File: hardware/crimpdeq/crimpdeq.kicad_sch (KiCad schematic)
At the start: 54 parts, among them J2 USB4105-GF-A, Q1 S8550, Q2 DMG3415U, SW1 SW_Push, SW2 SW_Push, U1 ESP32-C3-MINI-1, U2 MCP73831T-2ACI/OT, U3 HX711, U4 Rust_Board, U6 SY8088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

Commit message: pcb: Initial PCB design
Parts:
- C10, C11, C12, C13, C9: footprint (none) -> Capacitor_SMD:C_0603_1608Metric
- D3: footprint Rust_Board:SOD-882 -> Diode_SMD:D_SOD-882
- U1: footprint Espressif:ESP32-C3-MINI-1 -> PCM_Espressif:ESP32-C3-MINI-1
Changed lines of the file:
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@@
 			)
 		)
-		(property "Footprint" ""
+		(property "Footprint" "Capacitor_SMD:C_0603_1608Metric"
 			(at 41.6052 153.67 0)
 			(effects
@@
 			)
 		)
-		(property "Footprint" ""
+		(property "Footprint" "Capacitor_SMD:C_0603_1608Metric"
 			(at 58.1152 127 0)
 			(effects
@@
 			)
 		)
-		(property "Footprint" "Espressif:ESP32-C3-MINI-1"
+		(property "Footprint" "PCM_Espressif:ESP32-C3-MINI-1"
 			(at 85.09 86.36 0)
 			(effects
@@
 			)
 		)
-		(property "Footprint" ""
+		(property "Footprint" "Capacitor_SMD:C_0603_1608Metric"
 			(at 77.47 157.7848 0)
 			(effects
@@
 			)
 		)
-		(property "Footprint" ""
+		(property "Footprint" "Capacitor_SMD:C_0603_1608Metric"
 			(at 59.3852 140.97 0)
 			(effects
@@
 			)
 		)
-		(property "Footprint" ""
+		(property "Footprint" "Capacitor_SMD:C_0603_1608Metric"
 			(at 41.6052 166.37 0)
 			(effects
@@
 			)
 		)
-		(property "Footprint" "Rust_Board:SOD-882"
+		(property "Footprint" "Diode_SMD:D_SOD-882"
 			(at 25.4 87.63 0)
 			(effects

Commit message: pcb: Initial wiring of pcb
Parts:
- removed C13: 0.1uF, Capacitor_SMD:C_0603_1608Metric, symbol Device:C
- removed R8: 1kR 1%, Resistor_SMD:R_0402_1005Metric, symbol Device:R_Small_US
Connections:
- net B- is gone; now on net GND: U3.9 (INB-)
- net +BATT: now also U4.15 (VBAT), U4.21 (BAT+); no longer U4.28 (VBAT), U4.30 (BAT+)
- net A+: now also U4.16 (A+)
- net A-: now also U4.17 (A-)
- net ENABLE: now also U4.14 (ENABLE); no longer U4.27 (ENABLE)
- net GND: now also U3.10 (INB+), U4.18 (E-), U4.20 (BAT-); no longer U4.29 (BAT-)
- net IO0: no longer U1.12 (GPIO0/ADC1_CH0/XTAL_32K_P), U4.5 (A0/GPIO0)
- net IO1_ADC: now also U4.5 (A1/GPIO1); no longer U4.6 (A1/GPIO1)
- net IO20_RX: now also U4.9 (RXD/GPIO20); no longer U4.15 (RXD/GPIO20)
- net IO21_TX: now also U4.8 (TXD/GPIO21); no longer U4.14 (TXD/GPIO21)
- net IO4_DATA: now also U4.6 (A4/GPIO4); no longer U4.9 (A4/GPIO4)
- net IO5_SCK: now also U4.7 (A5/GPIO5); no longer U4.10 (A5/GPIO5)
- net IO9_BOOT: now also U4.10 (BOOT/GPIO9); no longer U4.16 (BOOT/GPIO9)
- net USB_D+: now also U4.11 (USB_D+/GPIO19); no longer U4.19 (USB_D+/GPIO19)
- net USB_D-: now also U4.12 (USB_D-/GPIO18); no longer U4.20 (USB_D-/GPIO18)
- net VBUS: now also U4.13 (VBUS); no longer U4.26 (VBUS)
- net E+: now reaches C10.1, Q1.3 (C), R5.1, U3.3 (AVDD)
- net E+: now also U4.19 (E+)
- net IO10: no longer names the net of U1.16 (GPIO10)
- net IO10: no longer U4.17 (SDA/GPIO10)
- net IO2: no longer names the net of U1.5 (GPIO2/ADC1_CH2)
- net IO2: no longer U4.7 (A2/GPIO2)
- net IO3: no longer names the net of U1.6 (GPIO3/ADC1_CH3)
- net IO3: no longer U4.8 (A3/GPIO3)
- net IO6: no longer names the net of U1.20 (GPIO6)
- net IO6: no longer U4.11 (GPIO6)
- net IO7: no longer names the net of U1.21 (GPIO7)
- net IO7: no longer U4.12 (GPIO7)
- removed net IO8: U1.22 (GPIO8), U4.13 (GPIO8), U4.18 (SCL/GPIO8)
- no-connect marks 9 -> 11

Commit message: pcb: Remove unused exposed pins and connect hx711/RATE to 3.3v
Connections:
- net +3.3V is gone; now on net +3V3: C9.1, Q1.1 (E), U3.1 (VSUP), U3.16 (DVDD)
- net +3V3: now also U3.15 (RATE), U4.1 (3V3); no longer U4.2 (3V3)
- net +BATT: now also U4.11 (VBAT), U4.17 (BAT+); no longer U4.15 (VBAT), U4.21 (BAT+)
- net A+: now also U4.12 (A+); no longer U4.16 (A+)
- net A-: now also U4.13 (A-); no longer U4.17 (A-)
- net CHIP_PU: no longer U4.1 (RST)
- net E+: now also U4.15 (E+); no longer U4.19 (E+)
- net ENABLE: no longer U4.14 (ENABLE)
- net GND: now also U4.14 (E-), U4.16 (BAT-), U4.2 (GND); no longer U3.15 (RATE), U4.18 (E-), U4.20 (BAT-), U4.4 (GND)
- net IO1_ADC: now also U4.3 (A1/GPIO1); no longer U4.5 (A1/GPIO1)
- net IO20_RX: now also U4.7 (RXD/GPIO20); no longer U4.9 (RXD/GPIO20)
- net IO21_TX: now also U4.6 (TXD/GPIO21); no longer U4.8 (TXD/GPIO21)
- net IO4_DATA: now also U4.4 (A4/GPIO4); no longer U4.6 (A4/GPIO4)
- net IO5_SCK: now also U4.5 (A5/GPIO5); no longer U4.7 (A5/GPIO5)
- net IO9_BOOT: no longer U4.10 (BOOT/GPIO9)
- net USB_D+: now also U4.9 (USB_D+/GPIO19); no longer U4.11 (USB_D+/GPIO19)
- net USB_D-: now also U4.8 (USB_D-/GPIO18); no longer U4.12 (USB_D-/GPIO18)
- net VBUS: now also U4.10 (VBUS); no longer U4.13 (VBUS)

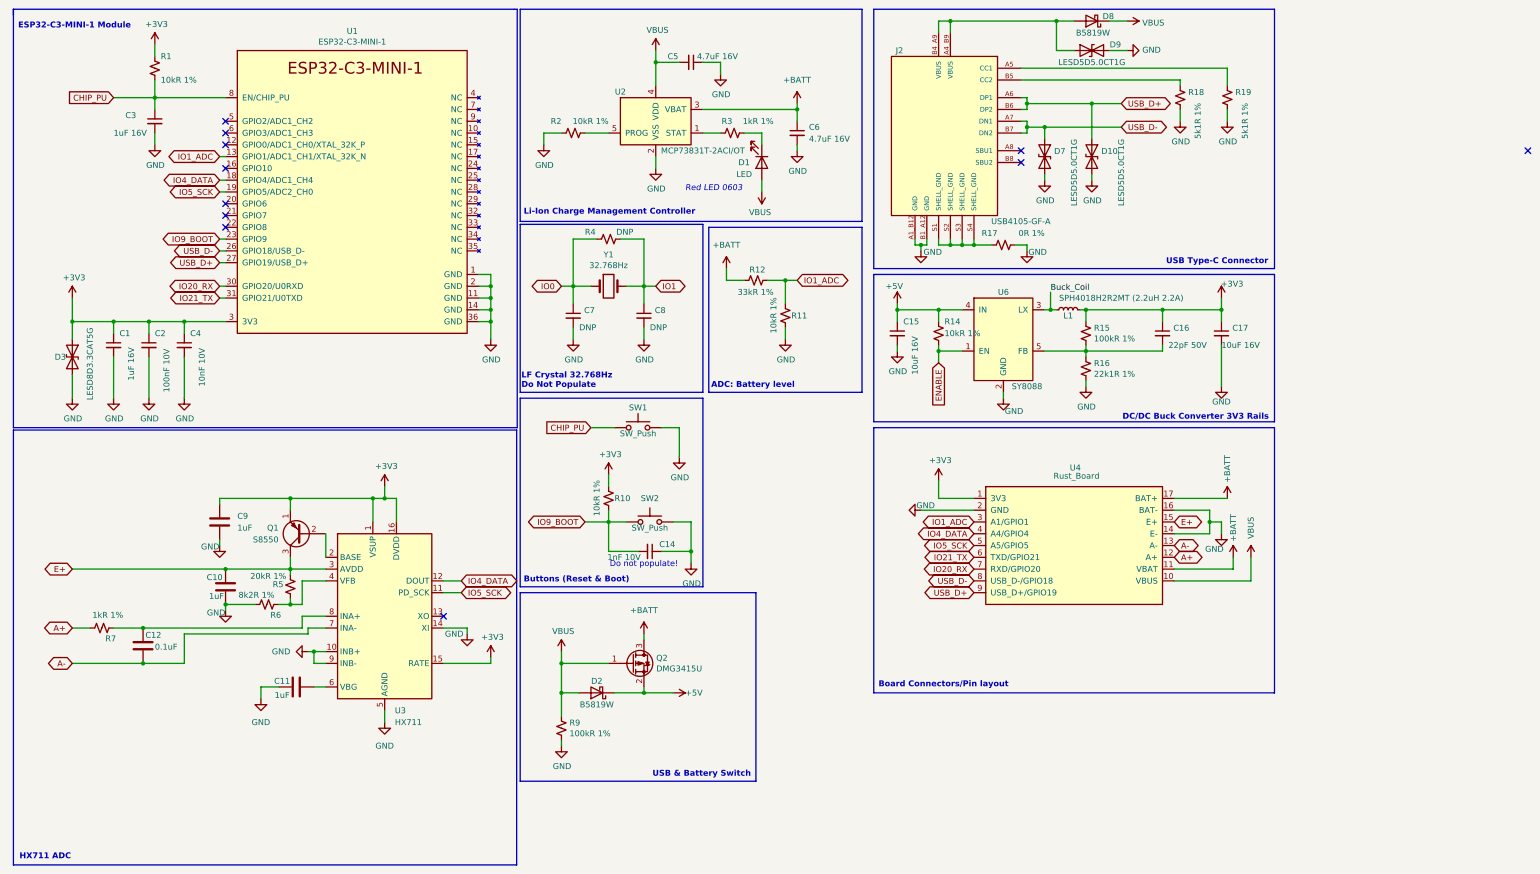
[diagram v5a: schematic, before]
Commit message: feat: Update schematic with NAU7802
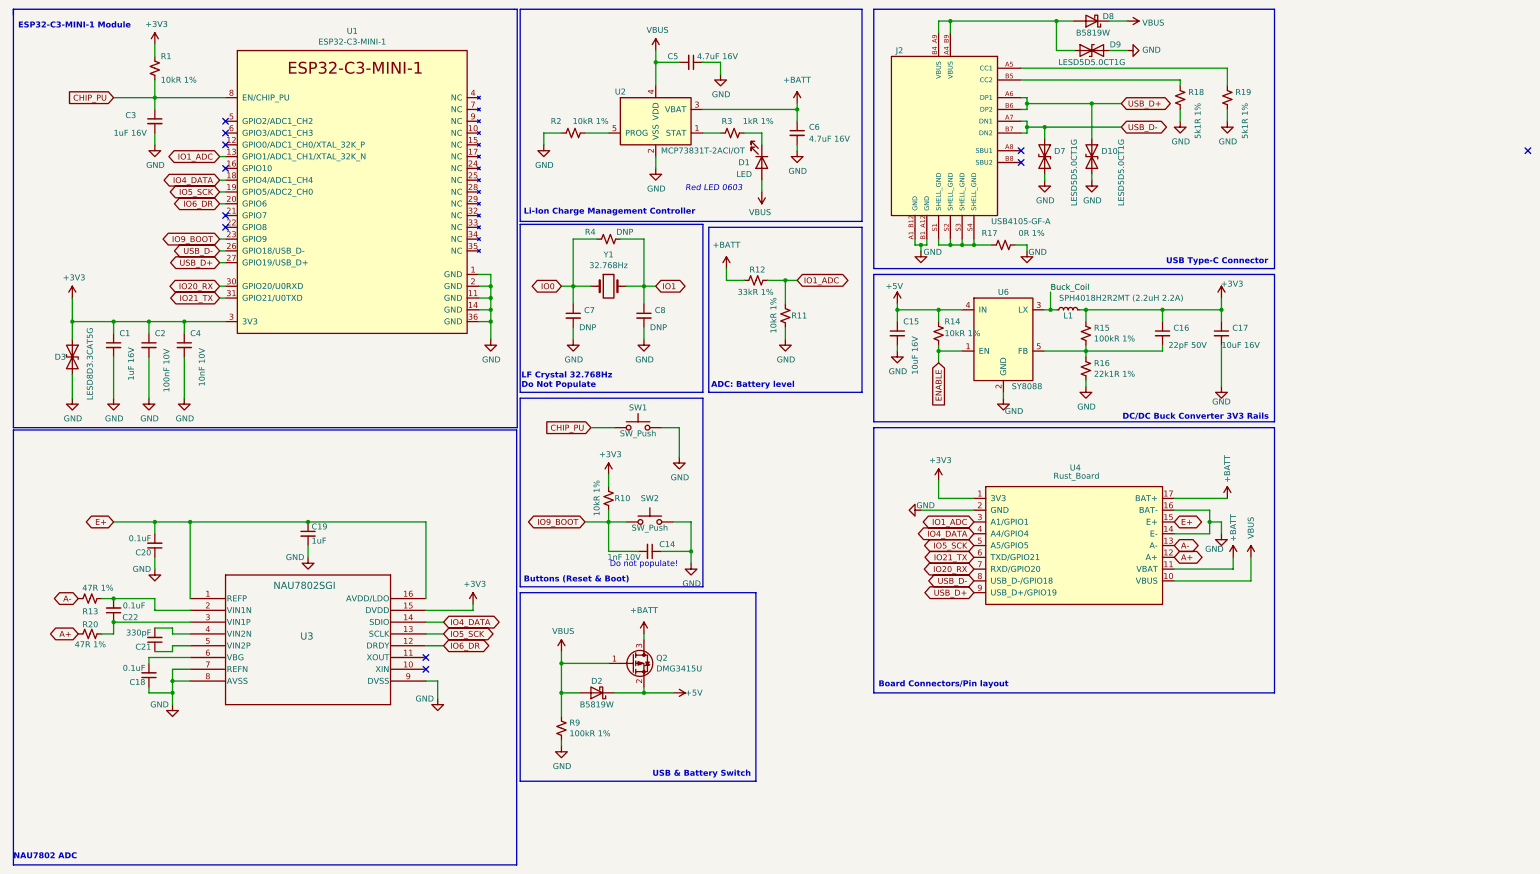
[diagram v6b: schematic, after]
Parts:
- removed C10, C11, C9: 1uF, Capacitor_SMD:C_0603_1608Metric, symbol Device:C
- removed C12: 0.1uF, Capacitor_SMD:C_0603_1608Metric, symbol Device:C
- removed Q1: S8550, Package_TO_SOT_THT:TO-92_Inline, symbol Transistor_BJT:S8550
- removed R5: 20kR 1%, Resistor_SMD:R_0402_1005Metric, symbol Device:R_Small_US
- removed R6: 8k2R 1%, Resistor_SMD:R_0402_1005Metric, symbol Device:R_Small_US
- removed R7: 1kR 1%, Resistor_SMD:R_0402_1005Metric, symbol Device:R_Small_US
- removed U3: HX711, Package_SO:SOP-16_3.9x9.9mm_P1.27mm, symbol Analog_ADC:HX711
- added C18, C20, C22: 0.1uF, Capacitor_SMD:C_0402_1005Metric, symbol Device:C_Small
- added C19: 1uF, Capacitor_SMD:C_0402_1005Metric, symbol Device:C_Small
- added C21: 330pF, Capacitor_SMD:C_0402_1005Metric, symbol Device:C_Small
- added R13, R20: 47R 1%, Resistor_SMD:R_0402_1005Metric, symbol Device:R_Small_US
- added U3: NAU7802SGI, SOI16_NAU7802SGI_NUV, symbol NAU7802SGI:NAU7802SGI
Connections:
- net +3V3: now also U3.15 (DVDD)
- net A+: now also R20.1
- net A-: now also R13.1
- net E+: now also C19.1, C20.2, U3.1 (REFP), U3.16 (AVDD/LDO)
- net GND: now also C18.1, C19.2, C20.1, U3.7 (REFN), U3.8 (AVSS), U3.9 (DVSS)
- net IO4_DATA: now also U3.14 (SDIO)
- net IO5_SCK: now also U3.13 (SCLK)
- net IO6_DR: now reaches U1.20 (GPIO6)
- net IO6_DR: now also U3.12 (DRDY)
- new net: C22.2, R13.2, U3.2 (VIN1N)
- new net: C22.1, R20.2, U3.3 (VIN1P)
- new net: C21.2, U3.4 (VIN2N)
- new net: C21.1, U3.5 (VIN2P)
- new net: C18.2, U3.6 (VBG)
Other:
- note added: "NAU7802 ADC"
- note removed: "HX711 ADC"
